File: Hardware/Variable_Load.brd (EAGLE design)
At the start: 125.7 x 41.9 mm, 51 parts, among them Q1 60V/32A/35mΩ, U1 CY8C5868LTI-LP039, U2 3.3V

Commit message: Made into a two-layer design
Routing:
- net 3.3V: track 27.8 -> 5.43 mm, vias 2 -> 0
- added copper zone on layer 16, net N$12
- removed copper zone on layer 15, net 5V
- removed copper zone on layer 2, net GND
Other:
- board text removed: "2"
- board text removed: "3"

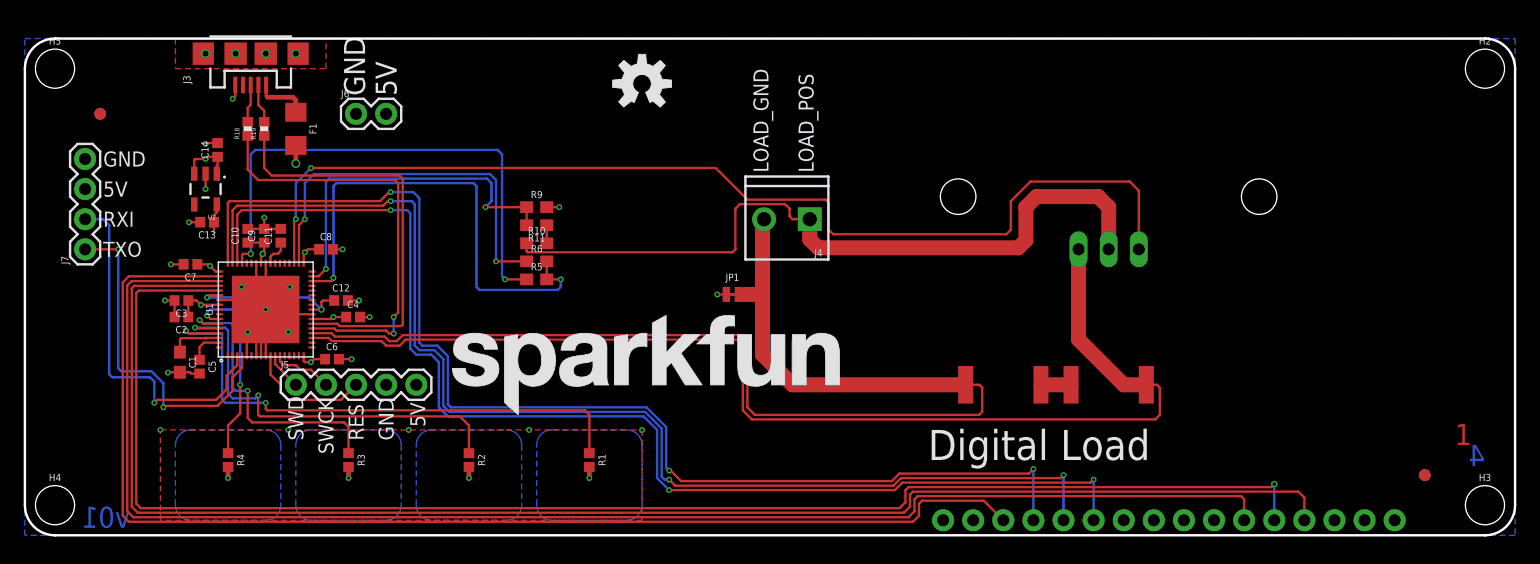
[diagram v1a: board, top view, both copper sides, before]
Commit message: Corrections from QC double check
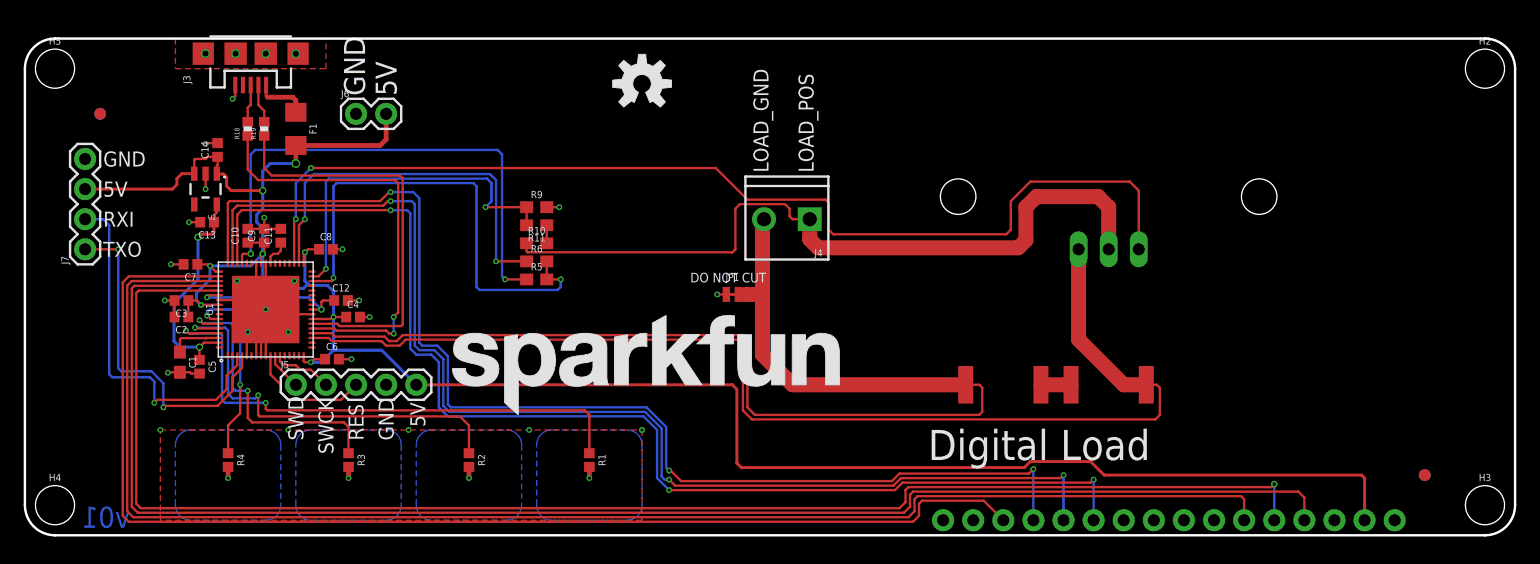
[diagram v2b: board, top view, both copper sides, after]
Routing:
- net 5V: track 23.4 -> 186.0 mm
- net 3.3V: track 5.43 -> 18.8 mm, vias 0 -> 2
- net GND: track 51.8 -> 55.2 mm
- added copper zone on layer 16, net GND
- removed copper zone on layer 16, net N$12
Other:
- board text added: "DO NOT CUT"
- board text added: "Dimensions In Inches"
- board text added: "Mike Hord"
- board text removed: "1"
- board text removed: "4"

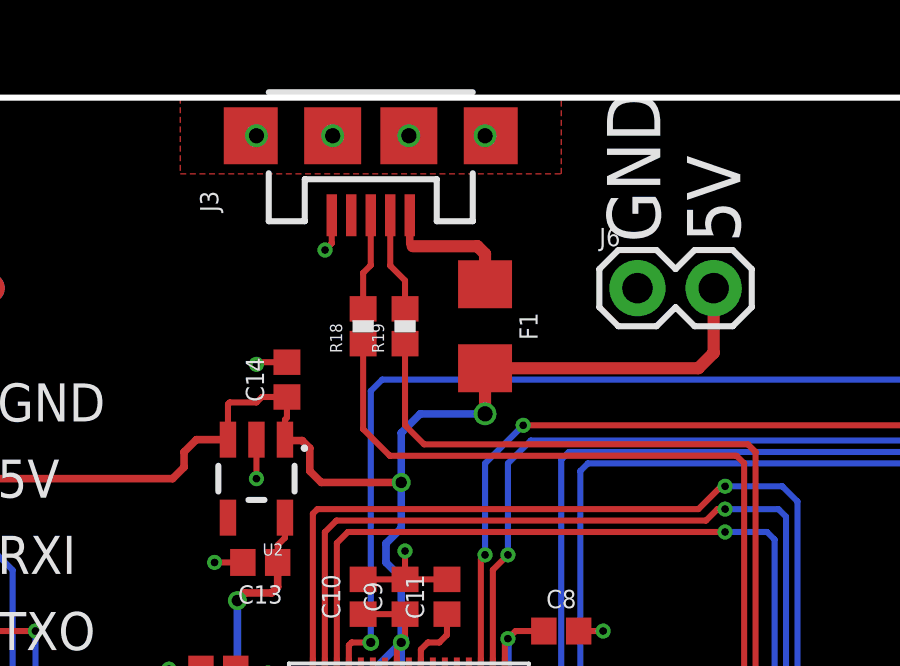
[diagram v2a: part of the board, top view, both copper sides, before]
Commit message: Replace USB jack with newer, bossed design
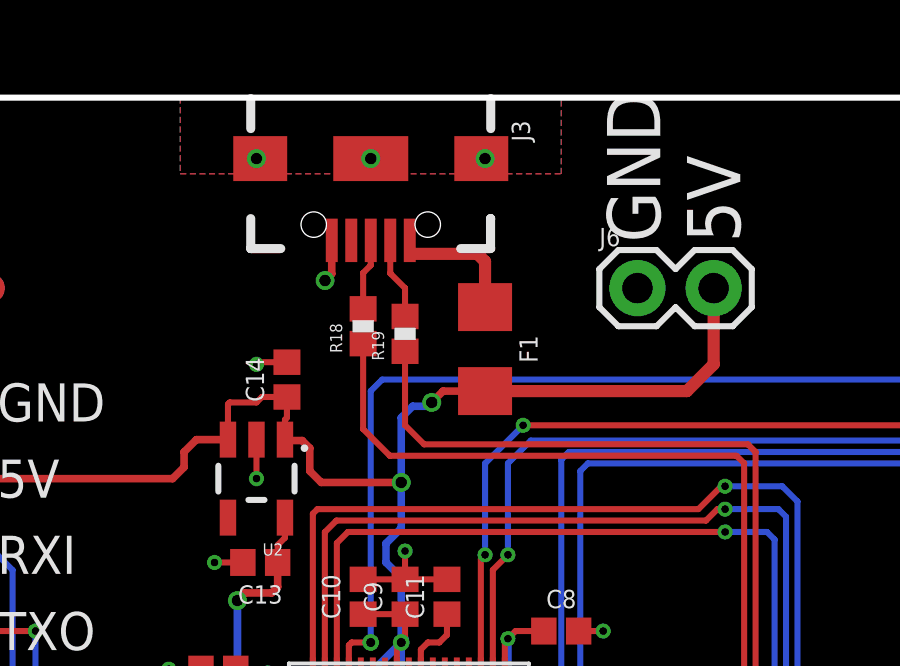
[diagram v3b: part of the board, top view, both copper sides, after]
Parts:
- J3: device SparkFun-Connectors:USB-MICROB -> SparkFun-Connectors:USB-B-MICRO-SMD
- moved F1 0.76 mm to (22.9, 33.5)
- moved J3 0.76 mm to (19.1, 39.9), turned to 270 degrees
- moved R19 0.25 mm to (20.2, 34.0)
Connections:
- net SHIELD: now also J3.SHIELD1, J3.SHIELD2, J3.SHIELD3; no longer J3.MT1, J3.MT2, J3.P$1, J3.P$2
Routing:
- net D+: track 3.23 -> 2.39 mm
- net D-: track 3.32 -> 2.74 mm
- added copper zone on layer 16, net SHIELD

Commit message: Add firmware, latest changes to HW
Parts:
- added D1: GREEN, SparkFun-LED:LED-1206-BOTTOM
- added R12: 560, SparkFun-Resistors:0402
- moved H2 246.4 mm to (-123.2, 39.4), flipped to the bottom
- moved H3 246.4 mm to (-123.2, 2.54), flipped to the bottom
- moved FD1 236.2 mm to (-118.1, 5.08), flipped to the top
- moved FD3 236.2 mm to (-118.1, 5.08), flipped to the bottom
- moved J2 231.1 mm to (-115.6, 1.27), flipped to the top
- moved H1 182.9 mm to (-91.4, 28.6), flipped to the top
- moved Q1 182.9 mm to (-91.4, 24.1), flipped to the top
- moved R7 182.9 mm to (-91.4, 12.7), flipped to the bottom
- moved R8 165.1 mm to (-82.5, 12.7), flipped to the bottom
- moved J4 132.1 mm to (-66.0, 26.7), flipped to the bottom
- moved LOGO3 132.1 mm to (-66.0, 31.8), flipped to the top
- moved JP1 119.4 mm to (-59.7, 20.3), flipped to the bottom
- moved LOGO1 104.1 mm to (-52.1, 38.1), flipped to the bottom
- moved R1 95.2 mm to (-47.6, 6.35), flipped to the bottom
- moved R10 86.4 mm to (-43.2, 24.6), flipped to the bottom
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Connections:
- new net N$12: D1.A, U1.29
- new net N$13: D1.C, R12.1
- net GND: now also R12.2
- net GND-ISO: now also U1.19; no longer U1.21
- net I_SENSE_HIGH: now also U1.18; no longer U1.20
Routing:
- net N$12: track 0.00 -> 15.3 mm, vias 0 -> 2
- net N$13: track 0.00 -> 2.70 mm
- net GND: track 55.4 -> 56.7 mm, vias 24 -> 25
- added copper zone on layer 1, net BACK
- added copper zone on layer 1, net DOWN
- added copper zone on layer 1, net ENTER
- added copper zone on layer 1, net UP
- removed copper zone on layer 16, net BACK
- removed copper zone on layer 16, net DOWN
- removed copper zone on layer 16, net ENTER
- removed copper zone on layer 16, net UP
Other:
- board text added: "ON"
- board text added: "v10"
- board text removed: "Digital Load"
- board text removed: "v01"

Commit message: Changes from design review
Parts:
- J3: value (none) -> AMP FCI 10103594-0001LF; device SparkFun-Connectors:USB-B-MICRO-SMD -> SparkFun-Connectors:USB-MICROB-PTH
- moved H2 246.4 mm to (123.2, 39.4), flipped to the top
- moved H3 246.4 mm to (123.2, 2.54), flipped to the top
- moved FD1 236.2 mm to (118.1, 5.08), flipped to the bottom
- moved FD3 236.2 mm to (118.1, 5.08), flipped to the top
- moved J2 231.1 mm to (115.6, 1.27), flipped to the bottom
- moved H1 182.9 mm to (91.4, 28.6), flipped to the bottom
- moved Q1 182.9 mm to (91.4, 24.1), flipped to the bottom
- moved R7 182.9 mm to (91.4, 12.7), flipped to the top
- moved R8 165.1 mm to (82.5, 12.7), flipped to the top
- moved J4 132.1 mm to (66.0, 26.7), flipped to the top
- moved LOGO3 132.1 mm to (66.0, 31.8), flipped to the bottom
- moved JP1 119.4 mm to (59.7, 20.3), flipped to the top
- moved LOGO1 104.1 mm to (52.1, 38.1), flipped to the top
- moved R1 95.2 mm to (47.6, 6.35), flipped to the top
- moved R10 86.4 mm to (43.2, 24.6), flipped to the top
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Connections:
- net SHIELD: now also J3.P$1, J3.P$10, J3.P$12, J3.P$2, J3.P$3, J3.P$4, J3.P$6, J3.P$8, J3.SHEILD2, J3.SHIELD, J3.SHIELD4; no longer J3.SHIELD1, J3.SHIELD2
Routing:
- net SHIELD: track 0.00 -> 30.9 mm, vias 3 -> 4
- net D-: track 2.74 -> 3.26 mm
- added copper zone on layer 16, net BACK
- added copper zone on layer 16, net DOWN
- added copper zone on layer 16, net ENTER
- added copper zone on layer 16, net UP
- removed copper zone on layer 1, net BACK
- removed copper zone on layer 1, net DOWN
- removed copper zone on layer 1, net ENTER
- removed copper zone on layer 1, net UP
